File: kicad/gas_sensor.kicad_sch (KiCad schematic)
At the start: 6 parts, among them U1 WeMos_D1_mini, U2 MQ-2, U3 DHT11, U4 DS3231M

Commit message: Update electric schema
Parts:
- added SW1: SW_Push, symbol Switch:SW_Push
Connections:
- net at BZ1.2, Brd1.1 (GND), U1.10 (GND)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: now also SW1.2
- net at U1.6 (MOSI/D7): now also SW1.1
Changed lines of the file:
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@@
 	(title_block
 		(title "ESP8266 gas detector alarm")
-		(date "2025-06-22")
+		(date "2026-01-11")
 		(rev "1")
 		(comment 1 "Franco Masotti")
 		(comment 2 "esp8266-iot-gas-detector")
-		(comment 3 "0.4.0")
+		(comment 3 "0.10.0")
+		(comment 4 "Pins referenced are NOT GPIOs but printed pins")
 	)
 	(junction
@@
 	)
 	(junction
+		(at 165.1 71.12)
+		(diameter 0)
+		(color 0 0 0 0)
+	)
+	(junction
 		(at 173.99 81.28)
 		(diameter 0)
@@
 	(wire
 		(pts
-			(xy 228.6 71.12) (xy 149.86 71.12)
-		)
-		(stroke
-			(width 0)
-			(type default)
-			(color 0 0 0 1)
-		)
-	)
-	(wire
-		(pts
 			(xy 165.1 110.49) (xy 165.1 119.38)
 		)
@@
 	(wire
 		(pts
+			(xy 165.1 71.12) (xy 149.86 71.12)
+		)
+		(stroke
+			(width 0)
+			(type default)
+			(color 0 0 0 1)
+		)
+	)
+	(wire
+		(pts
 			(xy 149.86 71.12) (xy 149.86 119.38)
 		)
@@
 	(wire
 		(pts
+			(xy 154.94 96.52) (xy 154.94 53.34)
+		)
+		(stroke
+			(width 0)
+			(type default)
+		)
+	)
+	(wire
+		(pts
+			(xy 165.1 53.34) (xy 165.1 71.12)
+		)
+		(stroke
+			(width 0)
+			(type default)
+			(color 0 0 0 1)
+		)
+	)
+	(wire
+		(pts
 			(xy 171.45 35.56) (xy 171.45 58.42)
 		)
@@
 	(wire
 		(pts
+			(xy 144.78 96.52) (xy 154.94 96.52)
+		)
+		(stroke
+			(width 0)
+			(type default)
+		)
+	)
+	(wire
+		(pts
 			(xy 149.86 119.38) (xy 165.1 119.38)
 		)
@@
 			(type default)
 			(color 0 237 255 1)
+		)
+	)
+	(wire
+		(pts
+			(xy 165.1 71.12) (xy 228.6 71.12)
+		)
+		(stroke
+			(width 0)
+			(type default)
+			(color 0 0 0 1)
 		)
 	)
@@
 					(unit 1)
 				)
+			)
+		)
+	)
+	(symbol
+		(lib_id "Switch:SW_Push")
+		(at 160.02 53.34 0)
+		(unit 1)
+		(exclude_from_sim no)
+		(in_bom yes)
+		(on_board yes)
+		(dnp no)
+		(property "Reference" "SW1"
+			(at 160.02 45.72 0)
+			(effects
+				(font
+					(size 1.27 1.27)
+				)
+			)
+		)
+		(property "Value" "SW_Push"
+			(at 160.02 48.26 0)
+			(effects
+				(font
+					(size 1.27 1.27)
+				)
+			)
+		)
+		(property "Footprint" ""
+			(at 160.02 48.26 0)
+			(effects
+				(font
+					(size 1.27 1.27)
+				)
+				(hide yes)
+			)
+		)
+		(property "Datasheet" "~"
+			(at 160.02 48.26 0)
+			(effects
+				(font
+					(size 1.27 1.27)
+				)
+				(hide yes)
+			)
+		)
+		(property "Description" "Push button switch, generic, two pins"
+			(at 160.02 53.34 0)
+			(effects
+				(font
+					(size 1.27 1.27)
+				)
+				(hide yes)
+			)
+		)
+		(property "Function" "Self test"
+			(at 160.02 53.34 0)
+			(effects
+				(font
+					(size 1.27 1.27)
+				)
+				(justify right bottom)
+			)
+		)
+		(pin "1"
+		)
+		(pin "2"
+		)
+		(instances
+			(project ""
+				(path "/74195df6-15d5-47d4-9be6-1fd474b469e5"
+					(reference "SW1")
+					(unit 1)
+				)

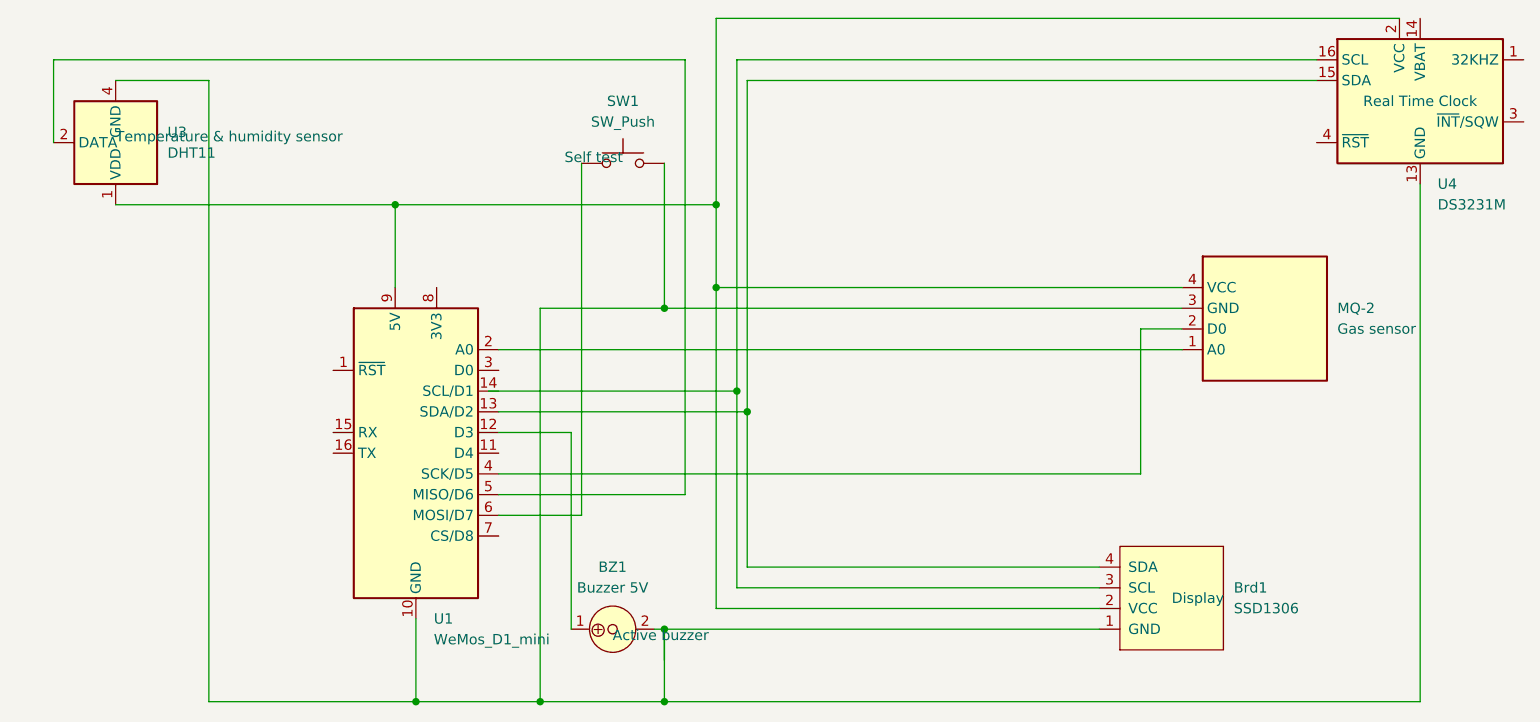
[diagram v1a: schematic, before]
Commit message: Split code into modules
- Add pin triggers.
- Improve logic and delays.
- Improve trigger mode output.
- Loop through triggers.
- Don't wait for MQ-* to heat up in setup, use loop.
- Initial support for function-based unit tests.
- Add basic pomodoro timer support.
- Fix pin definitions.
- Cleanup and fix documentation.
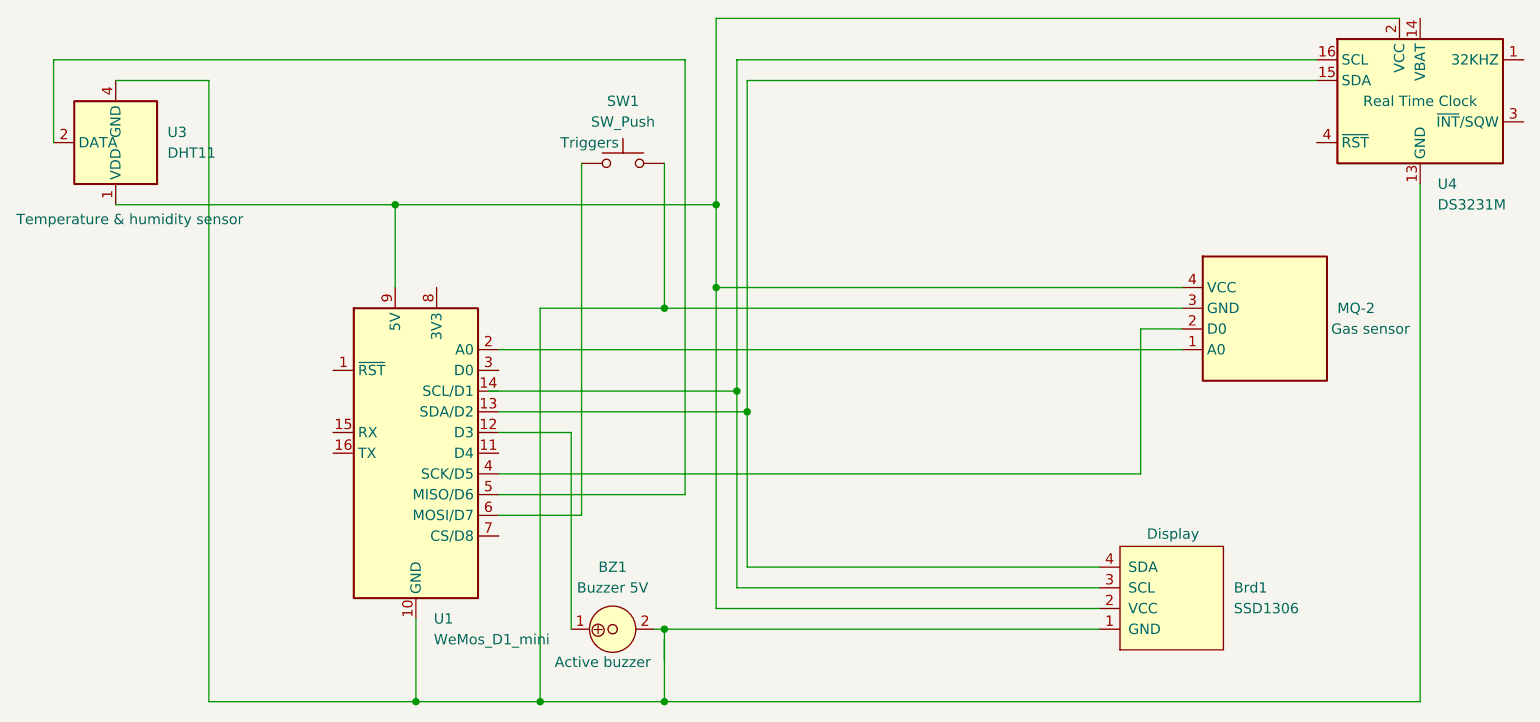
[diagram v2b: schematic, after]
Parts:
- SW1: Function Self test -> Triggers
